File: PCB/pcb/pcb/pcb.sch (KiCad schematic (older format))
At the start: 8 parts, among them P1 Conn_02x20_Odd_Even

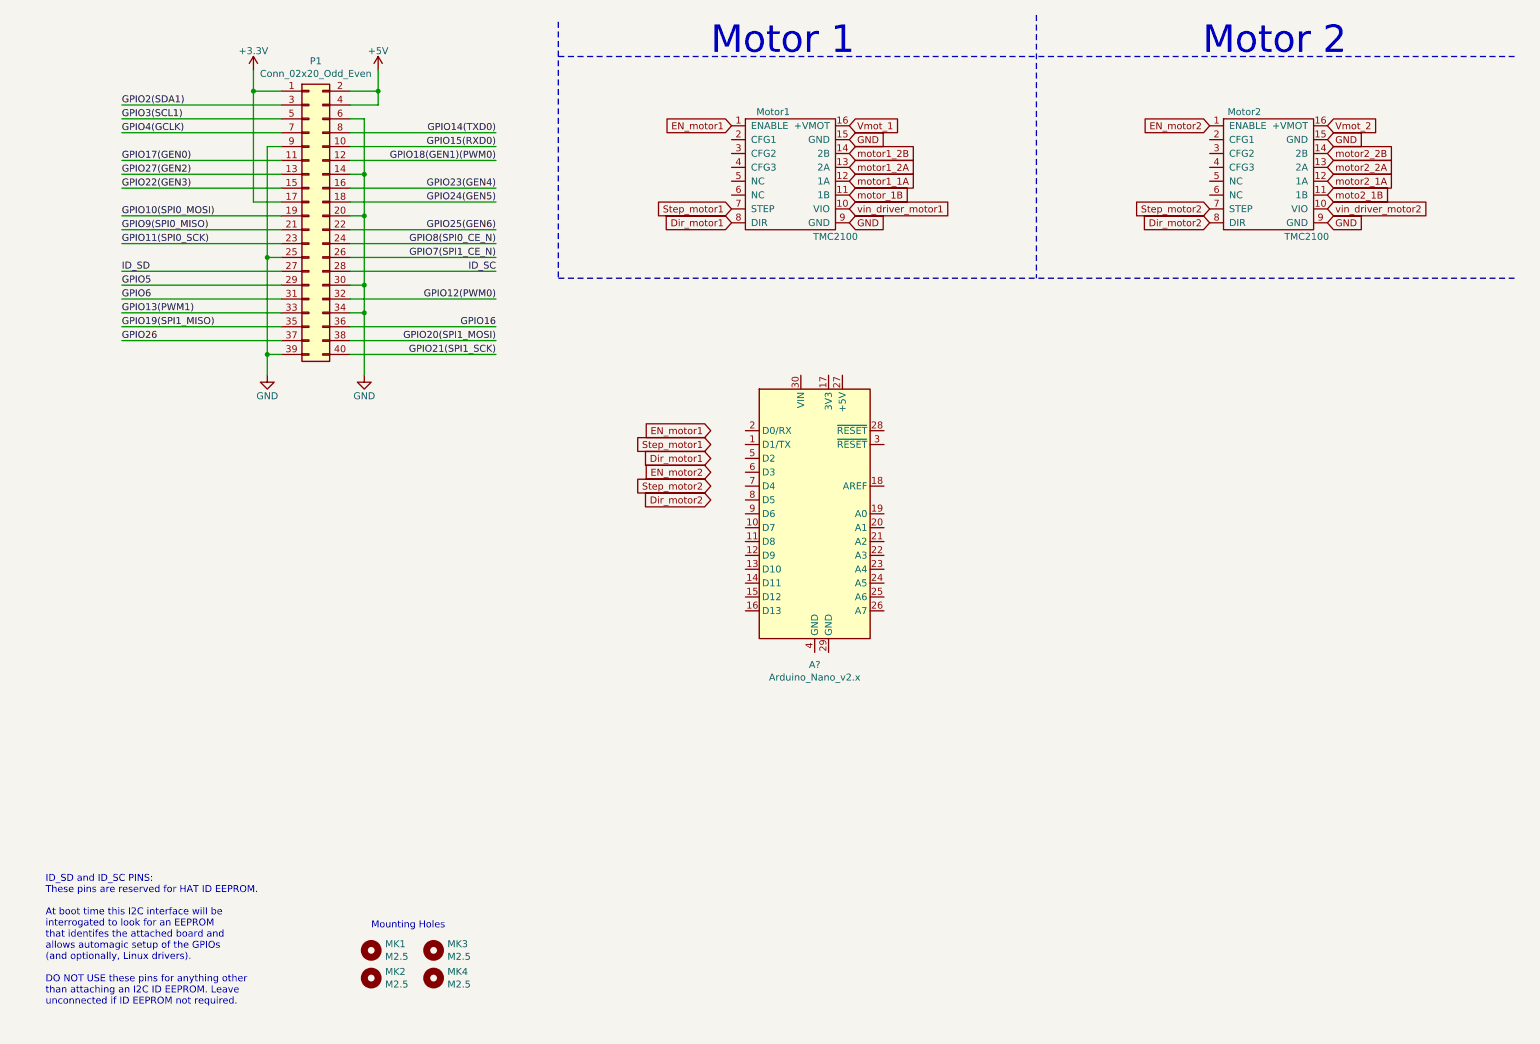
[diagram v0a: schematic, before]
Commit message: V0.7 finish the schematic that close #4
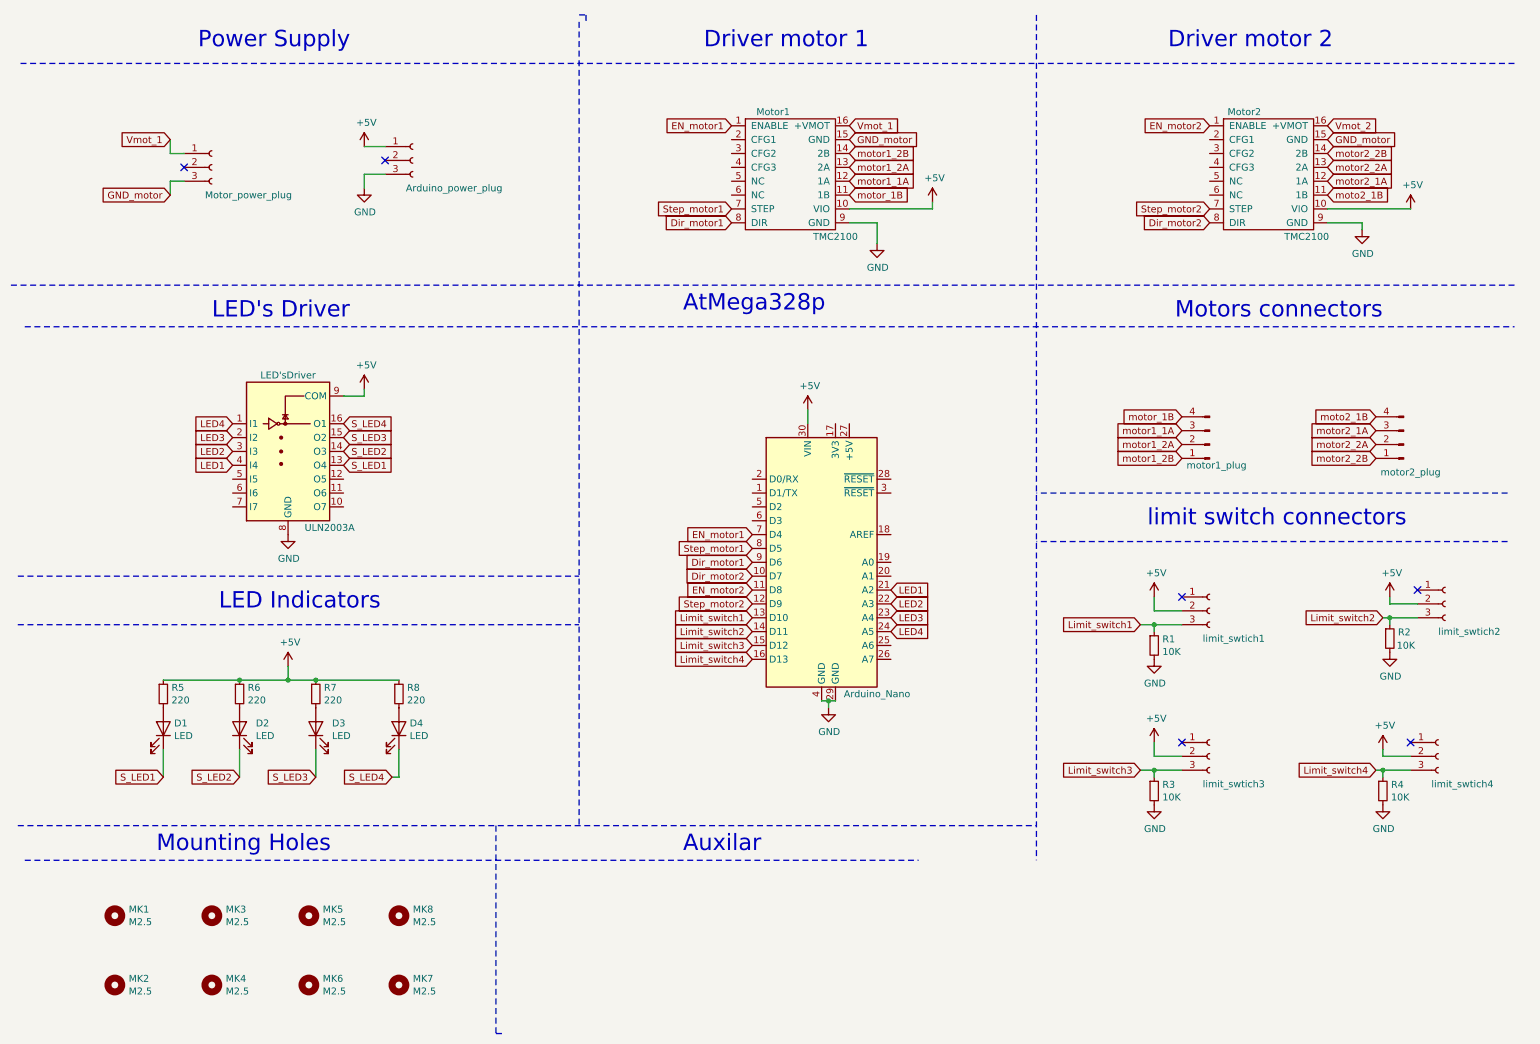
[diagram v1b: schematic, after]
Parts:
- removed P1: Conn_02x20_Odd_Even, Connector_PinSocket_2.54mm:PinSocket_2x20_P2.54mm_Vertical, symbol Connector_Generic:Conn_02x20_Odd_Even
- added Arduino_power_plug, Motor_power_plug, limit_swtich1, limit_swtich2, limit_swtich3, limit_swtich4: Conn_01x03_Female, symbol Connector:Conn_01x03_Female
- added D1, D2, D3, D4: LED, symbol Device:LED
- added LED'sDriver: ULN2003A, symbol Transistor_Array:ULN2003A
- added MK5, MK6, MK7, MK8: M2.5, MountingHole:MountingHole_2.7mm_M2.5, symbol pcb-rescue:Mounting_Hole-Mechanical
- added R1, R2, R3, R4: 10K, symbol Device:R_Small
- added R5, R6, R7, R8: 220, symbol Device:R_Small
- added motor1_plug, motor2_plug: Conn_01x04_Male, symbol Connector:Conn_01x04_Male
- gave numbers to parts that had none: 1
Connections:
- net vin_driver_motor1 is gone; now on net +5V: Motor1.10 (VIO)
- net vin_driver_motor2 is gone; now on net +5V: Motor2.10 (VIO)
- net +5V: now also Arduino_Nano.30 (VIN), Arduino_power_plug.1 (Pin_1), LED'sDriver.9 (COM), R5.1, R6.1, R7.1, R8.1, limit_swtich1.2 (Pin_2), limit_swtich2.2 (Pin_2), limit_swtich3.2 (Pin_2), limit_swtich4.2 (Pin_2)
- net Dir_motor1: now also Arduino_Nano.9 (D6)
- net Dir_motor2: now also Arduino_Nano.10 (D7)
- net EN_motor1: now also Arduino_Nano.7 (D4)
- net EN_motor2: now also Arduino_Nano.11 (D8)
- net GND: now also Arduino_Nano.29 (GND), Arduino_Nano.4 (GND), Arduino_power_plug.3 (Pin_3), LED'sDriver.8 (GND), R1.2, R2.2, R3.2, R4.2; no longer Motor1.15 (GND), Motor2.15 (GND)
- net Step_motor1: now also Arduino_Nano.8 (D5)
- net Step_motor2: now also Arduino_Nano.12 (D9)
- net Vmot_1: now also Motor_power_plug.1 (Pin_1)
- net moto2_1B: now also motor2_plug.4 (Pin_4)
- net motor1_1A: now also motor1_plug.3 (Pin_3)
- net motor1_2A: now also motor1_plug.2 (Pin_2)
- net motor1_2B: now also motor1_plug.1 (Pin_1)
- net motor2_1A: now also motor2_plug.3 (Pin_3)
- net motor2_2A: now also motor2_plug.2 (Pin_2)
- net motor2_2B: now also motor2_plug.1 (Pin_1)
- net motor_1B: now also motor1_plug.4 (Pin_4)
- net Limit_switch1: now reaches Arduino_Nano.13 (D10)
- net Limit_switch1: now also R1.1, limit_swtich1.3 (Pin_3)
- net Limit_switch2: now reaches Arduino_Nano.14 (D11)
- net Limit_switch2: now also R2.1, limit_swtich2.3 (Pin_3)
- net Limit_switch3: now reaches Arduino_Nano.15 (D12)
- net Limit_switch3: now also R3.1, limit_swtich3.3 (Pin_3)
- net Limit_switch4: now reaches Arduino_Nano.16 (D13)
- net Limit_switch4: now also R4.1, limit_swtich4.3 (Pin_3)
- net LED1: now reaches Arduino_Nano.21 (A2)
- net LED1: now also LED'sDriver.4 (I4)
- net LED2: now reaches Arduino_Nano.22 (A3)
- net LED2: now also LED'sDriver.3 (I3)
- net LED3: now reaches Arduino_Nano.23 (A4)
- net LED3: now also LED'sDriver.2 (I2)
- net LED4: now reaches Arduino_Nano.24 (A5)
- net LED4: now also LED'sDriver.1 (I1)
- new net: D3.2 (A), R7.2
- new net: D2.2 (A), R6.2
- new net: D1.2 (A), R5.2
- new net: D4.2 (A), R8.2
- new net GND_motor: Motor1.15 (GND), Motor2.15 (GND), Motor_power_plug.3 (Pin_3)
- new net S_LED1: D1.1 (K), LED'sDriver.13 (O4)
- new net S_LED2: D2.1 (K), LED'sDriver.14 (O3)
- new net S_LED3: D3.1 (K), LED'sDriver.15 (O2)
- new net S_LED4: D4.1 (K), LED'sDriver.16 (O1)
- no-connect marks 0 -> 6
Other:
- note added: "AtMega328p"
- note added: "Auxilar"
- note added: "Driver motor 1\n"
- note added: "Driver motor 2\n"
- note added: "LED Indicators"
- note added: "LED's Driver"
- note added: "Motors connectors"
- note added: "Mounting Holes\n"
- note added: "Power Supply"
- note added: "limit switch connectors"
- note removed: "ID_SD and ID_SC PINS:\nThese pins are reserved for HAT ID EEPROM.\n\nAt boot time this I2C interface will be\ninterrogated to look for an EEPROM\nthat identifes the attached board and\nallows automagic setup of the GPIOs\n(and optionally, Linux drivers).\n\nDO NOT USE these pins for anything other\nthan attaching an I2C ID EEPROM. Leave\nunconnected if ID EEPROM not required."
- note removed: "Motor 1\n"
- note removed: "Motor 2\n"
- note removed: "Mounting Holes"
- moved on the sheet: Arduino_Nano, MK1, MK2, MK3, MK4

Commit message: V0.75 all the footprints were set
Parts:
- Arduino_power_plug1: renamed from Arduino_power_plug; footprint (none) -> Connector_BarrelJack:BarrelJack_Horizontal
- D1, D2, D3, D4: footprint (none) -> LED_THT:LED_D3.0mm_FlatTop
- LED'sDriver1: renamed from LED'sDriver; footprint (none) -> Package_DIP:DIP-16_W7.62mm_LongPads
- Motor1, Motor2: footprint (none) -> Motor_driver:IC_DRV8825_STEPPER_MOTOR_DRIVER_CARRIER
- Motor_power_plug1: renamed from Motor_power_plug; footprint (none) -> Connector_BarrelJack:BarrelJack_Horizontal
- R1, R2, R3, R4, R5, R6, R7, R8: footprint (none) -> Resistor_THT:R_Axial_DIN0207_L6.3mm_D2.5mm_P7.62mm_Horizontal
- limit_swtich1, limit_swtich2, limit_swtich3, limit_swtich4: footprint (none) -> Connector_PinHeader_2.54mm:PinHeader_1x03_P2.54mm_Vertical
- motor1_plug1: renamed from motor1_plug; footprint (none) -> Connector_PinHeader_2.54mm:PinHeader_1x04_P2.54mm_Vertical
- motor2_plug1: renamed from motor2_plug; footprint (none) -> Connector_PinHeader_2.54mm:PinHeader_1x04_P2.54mm_Vertical
- renumbered Arduino_Nano to Arduino_Nano1
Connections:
- net Dir_motor1: now also Arduino_Nano1.7 (D4); no longer Arduino_Nano1.9 (D6)
- net EN_motor1: now also Arduino_Nano1.9 (D6); no longer Arduino_Nano1.7 (D4)
- net EN_motor2: now also Arduino_Nano1.12 (D9); no longer Arduino_Nano1.11 (D8)
- net Step_motor2: now also Arduino_Nano1.11 (D8); no longer Arduino_Nano1.12 (D9)

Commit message: V0.8 this commit close #5 also fixes #6
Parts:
- removed MK5, MK6, MK7, MK8: M2.5, MountingHole:MountingHole_2.7mm_M2.5, symbol pcb-rescue:Mounting_Hole-Mechanical
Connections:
- net Vmot_2 is gone; now on net Vmot_1: Motor2.16 (+VMOT)
- net LED1: now also LED'sDriver1.1 (I1); no longer LED'sDriver1.4 (I4)
- net LED2: now also LED'sDriver1.2 (I2); no longer LED'sDriver1.3 (I3)
- net LED3: now also LED'sDriver1.3 (I3); no longer LED'sDriver1.2 (I2)
- net LED4: now also LED'sDriver1.4 (I4); no longer LED'sDriver1.1 (I1)
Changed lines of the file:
@@
 GND_motor
 Text GLabel 9900 1250 2    50   Input ~ 0
-Vmot_2
+Vmot_1
 Text GLabel 9900 1550 2    50   Input ~ 0
 motor2_2A
@@
 Wire Wire Line
 	1550 1650 1550 1750
-$Comp
-L pcb-rescue:Mounting_Hole-Mechanical MK7
-U 1 1 5F8A5C55
-P 3200 7450
-F 0 "MK7" H 3300 7496 50  0000 L CNN
-F 1 "M2.5" H 3300 7405 50  0000 L CNN
-F 2 "MountingHole:MountingHole_2.7mm_M2.5" H 3200 7450 60  0001 C CNN
-F 3 "" H 3200 7450 60  0001 C CNN
-	1    3200 7450
-	1    0    0    -1
-$EndComp
-$Comp
-L pcb-rescue:Mounting_Hole-Mechanical MK6
-U 1 1 5F8A5C5B
-P 2550 7450
-F 0 "MK6" H 2650 7496 50  0000 L CNN
-F 1 "M2.5" H 2650 7405 50  0000 L CNN
-F 2 "MountingHole:MountingHole_2.7mm_M2.5" H 2550 7450 60  0001 C CNN
-F 3 "" H 2550 7450 60  0001 C CNN
-	1    2550 7450
-	1    0    0    -1
-$EndComp
-$Comp
-L pcb-rescue:Mounting_Hole-Mechanical MK8
-U 1 1 5F8A5C61
-P 3200 6950
-F 0 "MK8" H 3300 6996 50  0000 L CNN
-F 1 "M2.5" H 3300 6905 50  0000 L CNN
-F 2 "MountingHole:MountingHole_2.7mm_M2.5" H 3200 6950 60  0001 C CNN
-F 3 "" H 3200 6950 60  0001 C CNN
-	1    3200 6950
-	1    0    0    -1
-$EndComp
-$Comp
-L pcb-rescue:Mounting_Hole-Mechanical MK5
-U 1 1 5F8A5C67
-P 2550 6950
-F 0 "MK5" H 2650 6996 50  0000 L CNN
-F 1 "M2.5" H 2650 6905 50  0000 L CNN
-F 2 "MountingHole:MountingHole_2.7mm_M2.5" H 2550 6950 60  0001 C CNN
-F 3 "" H 2550 6950 60  0001 C CNN
-	1    2550 6950
-	1    0    0    -1
-$EndComp
 Wire Notes Line
 	500  2700 11250 2700
@@
 Text Notes 1850 2650 0    118  ~ 0
 LED's Driver
+Text GLabel 2000 3400 0    50   Input ~ 0
+LED1
+Text GLabel 2000 3500 0    50   Input ~ 0
+LED2
+Text GLabel 2000 3600 0    50   Input ~ 0
+LED3
 Text GLabel 2000 3700 0    50   Input ~ 0
-LED1
-Text GLabel 2000 3600 0    50   Input ~ 0
-LED2
-Text GLabel 2000 3500 0    50   Input ~ 0
-LED3
-Text GLabel 2000 3400 0    50   Input ~ 0
 LED4
 Text GLabel 2800 3700 2    50   Input ~ 0

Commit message: V0.8 pcb Finished this closes #9 and closes #8
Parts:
- removed MK2: M2.5, MountingHole:MountingHole_2.7mm_M2.5, symbol pcb-rescue:Mounting_Hole-Mechanical
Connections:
- net +5V: now also Arduino_Nano1.27 (+5V)
- net GND: now also Arduino_Nano1.26 (A7), Arduino_power_plug1.2 (Pin_2); no longer Arduino_Nano1.4 (GND)
- net GND_motor: now also Motor_power_plug1.2 (Pin_2)
- net Limit_switch1: now also Arduino_Nano1.19 (A0); no longer Arduino_Nano1.13 (D10)
- no-connect marks 6 -> 5
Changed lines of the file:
@@
 Wire Notes Line
 	11200 4250 7800 4250
-Text GLabel 5750 4800 0    50   Input ~ 0
+Text GLabel 6750 4400 2    50   Input ~ 0
 Limit_switch1
 Text GLabel 5750 5000 0    50   Input ~ 0
@@
 L power:GND #PWR0110
 U 1 1 5F7B1284
-P 6300 5450
-F 0 "#PWR0110" H 6300 5200 50  0001 C CNN
-F 1 "GND" H 6305 5277 50  0000 C CNN
-F 2 "" H 6300 5450 50  0001 C CNN
-F 3 "" H 6300 5450 50  0001 C CNN
-	1    6300 5450
-	1    0    0    -1
-$EndComp
-Wire Wire Line
-	6250 5400 6300 5400
-Wire Wire Line
-	6300 5450 6300 5400
-Connection ~ 6300 5400
-Wire Wire Line
-	6300 5400 6350 5400
-Wire Wire Line
-	6150 3300 6150 3400
+P 6350 5400
+F 0 "#PWR0110" H 6350 5150 50  0001 C CNN
+F 1 "GND" H 6355 5227 50  0000 C CNN
+F 2 "" H 6350 5400 50  0001 C CNN
+F 3 "" H 6350 5400 50  0001 C CNN
+	1    6350 5400
+	1    0    0    -1
+$EndComp
 $Comp
 L power:+5V #PWR0111
@@
 $EndComp
 $Comp
-L pcb-rescue:Mounting_Hole-Mechanical MK2
-U 1 1 5834FC19
-P 1150 7450
-F 0 "MK2" H 1250 7496 50  0000 L CNN
-F 1 "M2.5" H 1250 7405 50  0000 L CNN
-F 2 "MountingHole:MountingHole_2.7mm_M2.5" H 1150 7450 60  0001 C CNN
-F 3 "" H 1150 7450 60  0001 C CNN
-	1    1150 7450
-	1    0    0    -1
-$EndComp
-$Comp
 L pcb-rescue:Mounting_Hole-Mechanical MK3
 U 1 1 5834FBEF
@@
 Wire Wire Line
 	3100 1400 2950 1400
-NoConn ~ 3100 1500
 $Comp
 L Connector:Conn_01x03_Female Motor_power_plug1
@@
 	1    0    0    -1
 $EndComp
-NoConn ~ 1650 1550
 Wire Wire Line
 	1650 1450 1550 1450
@@
 Wire Notes Line
 	450  4850 4500 4850
+NoConn ~ 6250 5400
+Wire Wire Line
+	6150 3300 6150 3400
+Wire Wire Line
+	1650 1550 1650 1650
+Connection ~ 1650 1650
+Wire Wire Line
+	3100 1500 3100 1600
+Connection ~ 3100 1600
+$Comp
+L power:+5V #PWR0120
+U 1 1 5F6E3F0F
+P 6450 3300
+F 0 "#PWR0120" H 6450 3150 50  0001 C CNN
+F 1 "+5V" H 6465 3473 50  0000 C CNN
+F 2 "" H 6450 3300 50  0001 C CNN
+F 3 "" H 6450 3300 50  0001 C CNN
+	1    6450 3300
+	1    0    0    -1
+$EndComp
+Wire Wire Line
+	6450 3300 6450 3400
+$Comp
+L power:GND #PWR?
+U 1 1 5F6E7E9E
+P 6750 5100
+F 0 "#PWR?" H 6750 4850 50  0001 C CNN
+F 1 "GND" H 6755 4927 50  0000 C CNN
+F 2 "" H 6750 5100 50  0001 C CNN
+F 3 "" H 6750 5100 50  0001 C CNN
+	1    6750 5100
+	1    0    0    -1
+$EndComp
 $EndSCHEMATC

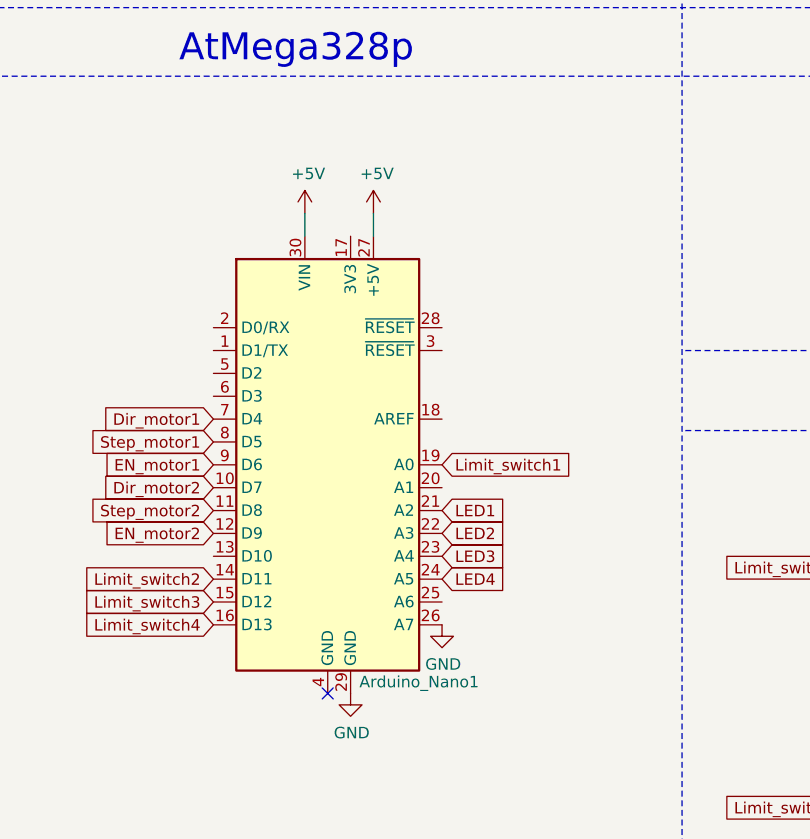
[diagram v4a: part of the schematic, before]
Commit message: V1.1 directions on arduino
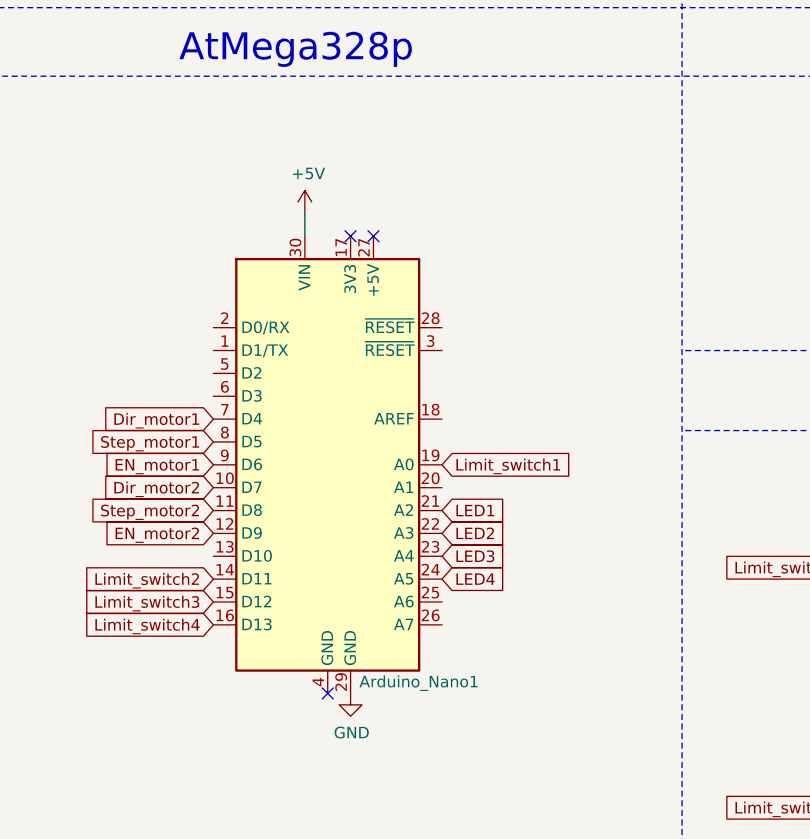
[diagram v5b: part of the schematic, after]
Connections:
- net +5V: no longer Arduino_Nano1.27 (+5V)
- net GND: no longer Arduino_Nano1.26 (A7)
- no-connect marks 5 -> 7
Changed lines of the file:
@@
 	3100 1500 3100 1600
 Connection ~ 3100 1600
-$Comp
-L power:+5V #PWR0120
-U 1 1 5F6E3F0F
-P 6450 3300
-F 0 "#PWR0120" H 6450 3150 50  0001 C CNN
-F 1 "+5V" H 6465 3473 50  0000 C CNN
-F 2 "" H 6450 3300 50  0001 C CNN
-F 3 "" H 6450 3300 50  0001 C CNN
-	1    6450 3300
-	1    0    0    -1
-$EndComp
-Wire Wire Line
-	6450 3300 6450 3400
-$Comp
-L power:GND #PWR?
-U 1 1 5F6E7E9E
-P 6750 5100
-F 0 "#PWR?" H 6750 4850 50  0001 C CNN
-F 1 "GND" H 6755 4927 50  0000 C CNN
-F 2 "" H 6750 5100 50  0001 C CNN
-F 3 "" H 6750 5100 50  0001 C CNN
-	1    6750 5100
-	1    0    0    -1
-$EndComp
+NoConn ~ 6450 3400
+NoConn ~ 6350 3400
 $EndSCHEMATC
